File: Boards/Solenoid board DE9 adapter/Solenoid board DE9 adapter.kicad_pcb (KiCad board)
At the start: 2 copper layers, 22.1 x 35.3 mm, 3 parts, among them J1 DE9_Plug_MountingHoles, J2 character connector

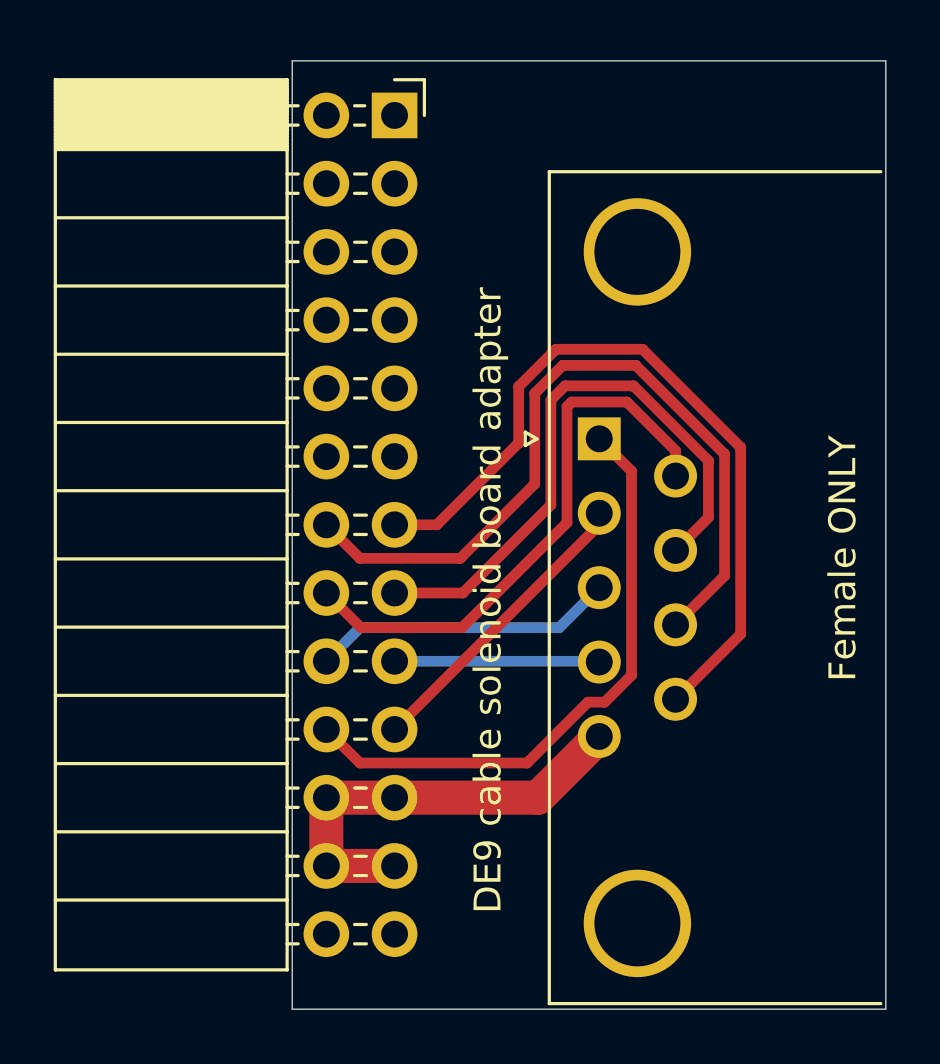
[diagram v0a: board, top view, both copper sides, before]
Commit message: added audio board schematics and de9 board fab files
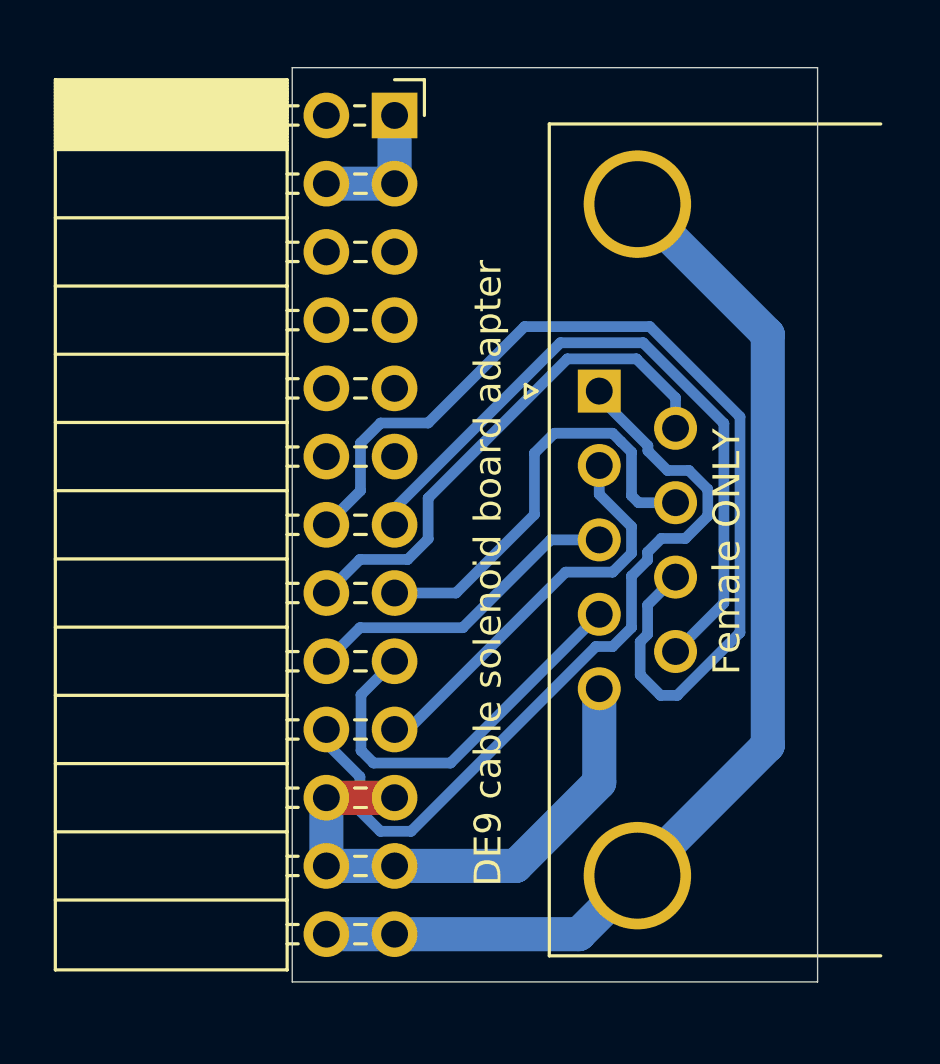
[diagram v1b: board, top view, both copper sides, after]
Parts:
- moved G*** 1.82 mm to (127.3, 97.5)
- moved J1 1.78 mm to (121.9, 106.8)
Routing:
- net 24R: track 0.00 -> 41.5 mm
- net CC7: track 28.8 -> 38.1 mm
- net CC4: track 7.63 -> 15.2 mm
- net CC1: track 22.5 -> 29.8 mm
- net CC6: track 22.2 -> 16.3 mm
- net SIGNAL GND.: track 0.00 -> 5.08 mm
- net CC2: track 11.2 -> 15.7 mm
- net +24VDC: track 16.2 -> 20.0 mm
- net CC8: track 28.7 -> 25.9 mm
- net CC5: track 21.2 -> 19.2 mm
- net CC3: track 11.3 -> 12.0 mm
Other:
- board size 22.1 x 35.3 mm -> 19.6 x 34 mm
